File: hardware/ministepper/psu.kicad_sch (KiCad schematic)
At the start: 13 parts, among them U2 TPS54061DRBT

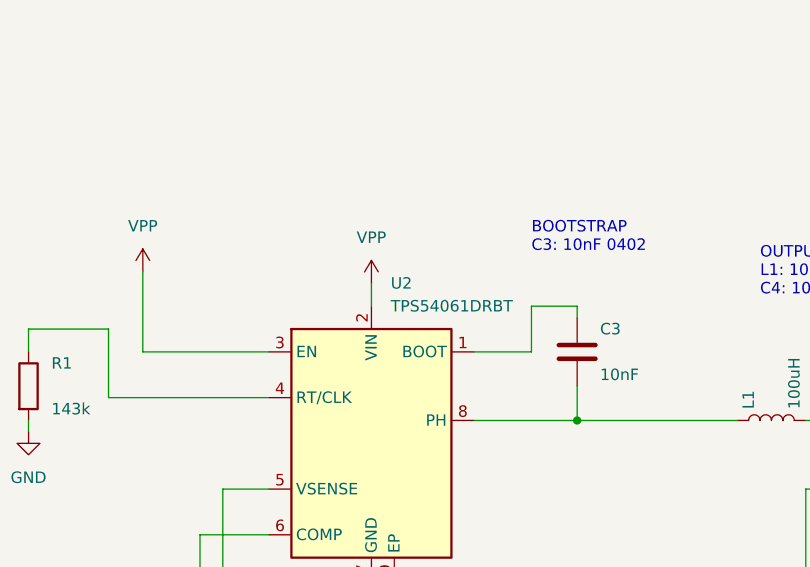
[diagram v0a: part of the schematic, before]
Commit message: ministepper: motor connectors (JMOT1, JMOT2) switch to vertical JST-XH
Was S4B-XH-A horizontal (right-angle, LCSC C157925) — now B4B-XH-A
vertical (top-mount, LCSC C595709, B4B-XH-A-R(LF)(SN), red housing
version, ~$0.08). The vertical variant keeps the motor cables exiting
straight up, which is usually more natural for stepper wiring vs the
board-edge horizontal style.

Bus connectors (JBUS1, JBUS2) and the optional external-power input
(JPWR) remain horizontal S*B-XH-A for board-edge cable exit.

Also regenerates docs + JLCPCB package.
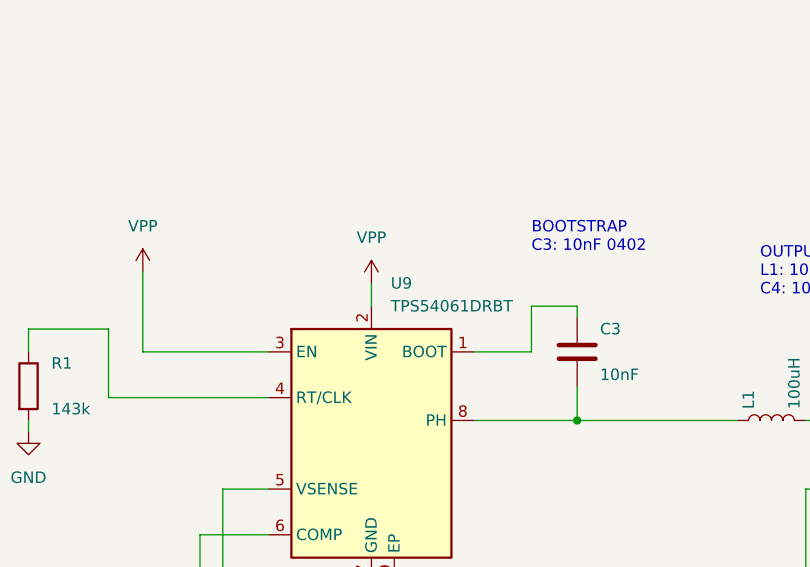
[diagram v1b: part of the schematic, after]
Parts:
- renumbered U2 to U9
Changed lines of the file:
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@@
 		(dnp no)
 		(fields_autoplaced yes)
-		(property "Reference" "U2"
+		(property "Reference" "U9"
 			(at 144.3833 77.47 0)
 			(show_name no)
@@
 			(project "ministepper"
 				(path "/e1d2c3b4-a5f6-7890-abcd-ef9876543210/f2e3d4c5-b6a7-8901-bcde-f09876543210"
-					(reference "U2")
+					(reference "U9")
 					(unit 1)
 				)
